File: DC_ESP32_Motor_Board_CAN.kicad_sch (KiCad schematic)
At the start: 44 parts, among them IC1 VNH7100BASTR, IC2 TJA1050T_CM, IC3 LSM6DS3TR-C, J1 SM04B-SRSS-TB, J2 SM04B-SRSS-TB, J3 XT30PB, J4 XT30PB, J5 SM04B-SRSS-TB, J6 SM04B-SRSS-TB, J7 XT30PB, J8 Conn_01x03_Pin, Q1 BSS138, Q2 BSS138, SW1 DSHP04TJGER, U1 MOUDLE-SEEEDUINO-XIAO-ESP32C3

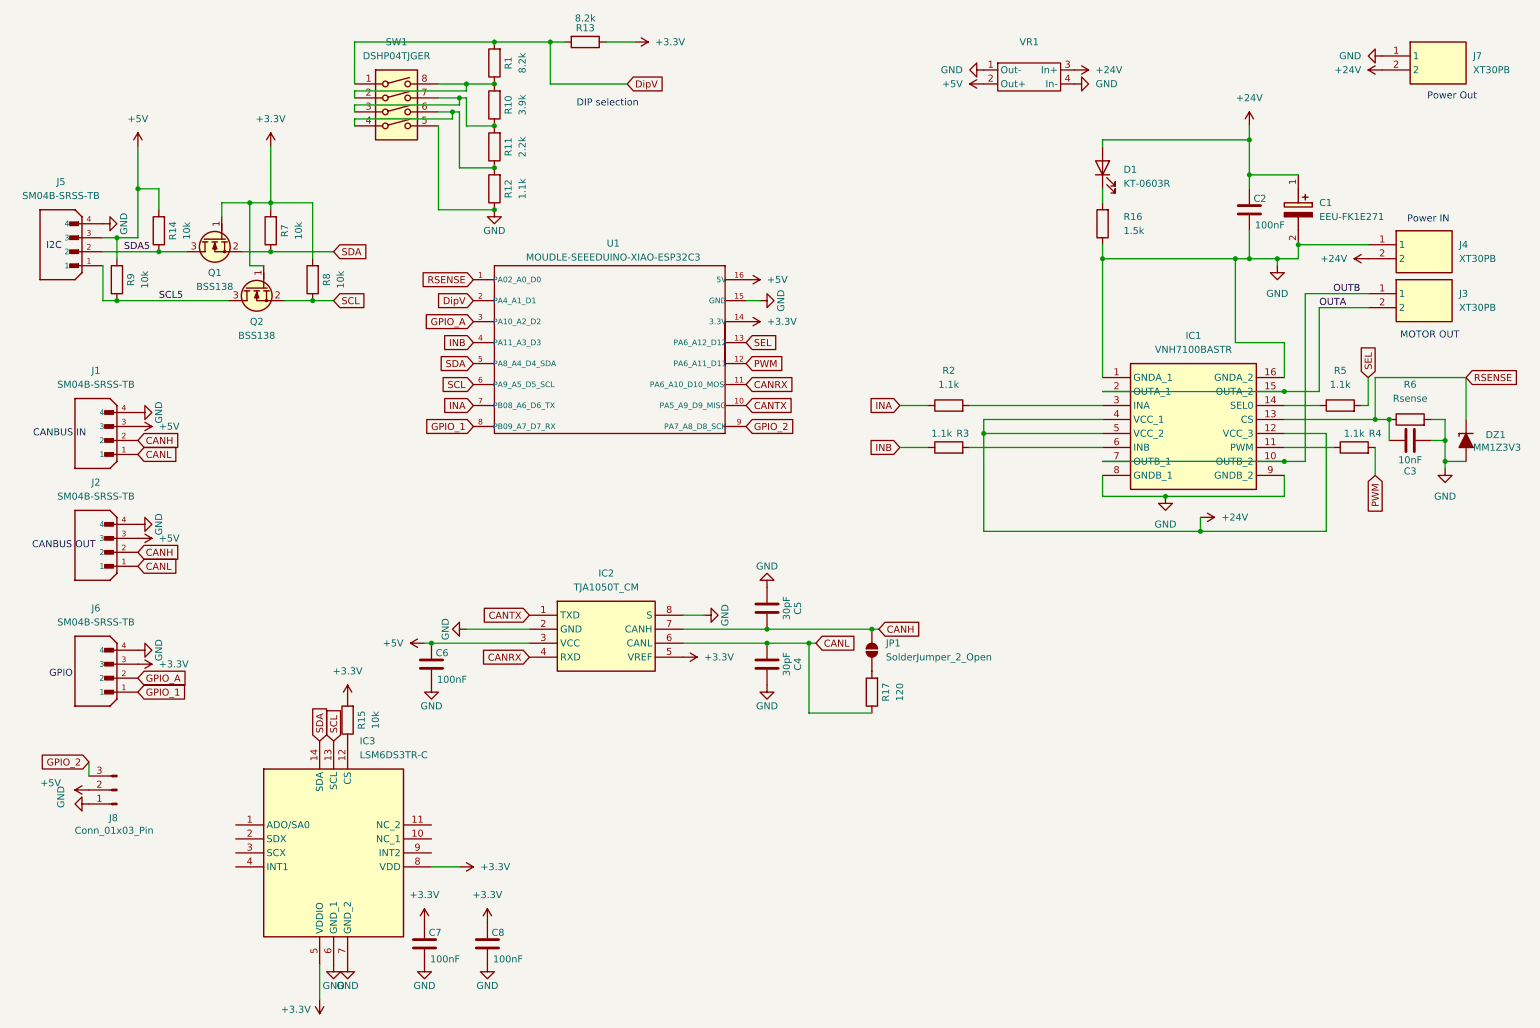
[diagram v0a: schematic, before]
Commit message: Updates for PCB
Bigger GPIO2
Added RGB LED
Updated xt30s
Updated xt30 size to fit inline connectors on PCB
Fixed jst sh connections
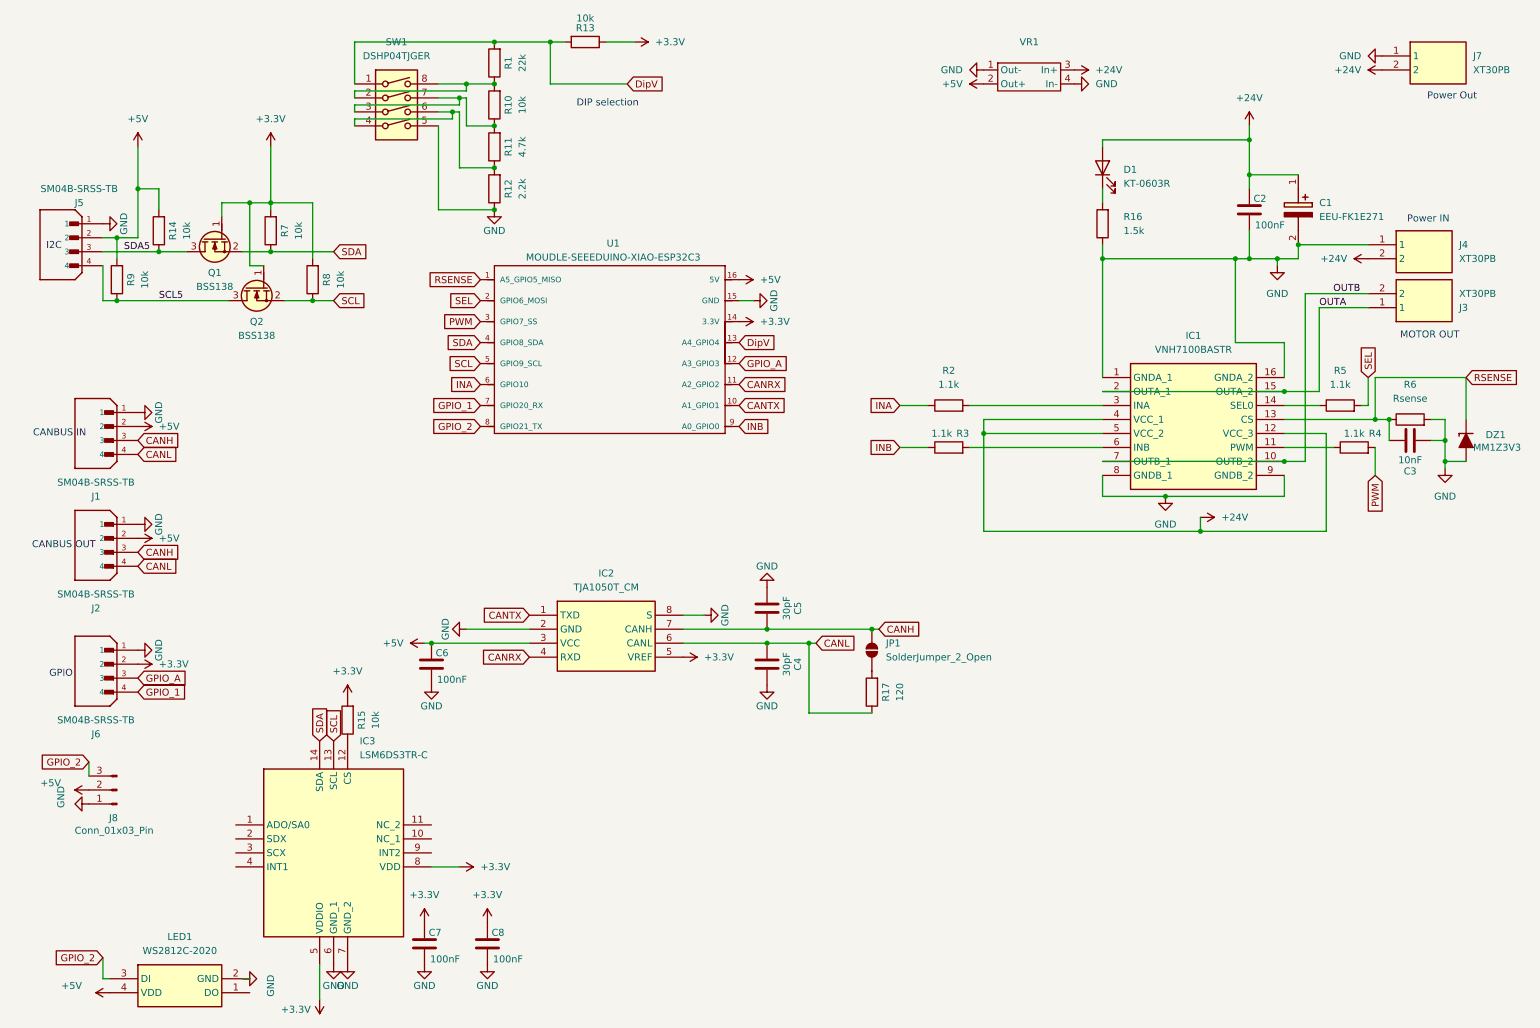
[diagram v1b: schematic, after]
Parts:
- added LED1: WS2812C-2020, WS2812C2020, symbol SamacSys_Parts:WS2812C-2020
- J3: footprint Library:Xt30 Horizontal -> JST_Sorted:Xt30 Female 90 1 mount removed
- J8: footprint Connector_PinHeader_1.00mm:PinHeader_1x03_P1.00mm_Vertical -> Connector_PinHeader_2.54mm:PinHeader_1x03_P2.54mm_Vertical
- R1: value 8.2k -> 22k
- R10: value 3.9k -> 10k
- R11: value 2.2k -> 4.7k
- R12: value 1.1k -> 2.2k
- R13: value 8.2k -> 10k
- U1: footprint Arduino:ESP32-C3 16 Pin Super Mini -> Arduino:MOUDLE14P-SMD-2.54-21X17.8MM; symbol SamacSys_Parts:MOUDLE-SEEEDUINO-XIAO-ESP32C3 -> SamacSys_Parts:ESP32_C3_Super_mini; now in the parts list
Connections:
- net +3.3V: now also J6.2; no longer J6.3
- net +5V: now also J1.2, J2.2, J5.2, LED1.4 (VDD); no longer J1.3, J2.3, J5.3
- net CANH: now also J1.3, J2.3; no longer J1.2, J2.2
- net CANL: now also J1.4, J2.4; no longer J1.1, J2.1
- net DipV: now also U1.13 (A4_GPIO4); no longer U1.2 (PA4_A1_D1)
- net GND: now also J1.1, J2.1, J5.1, J6.1, LED1.2 (GND); no longer J1.4, J2.4, J5.4, J6.4
- net GPIO_1: now also J6.4, U1.7 (GPIO20_RX); no longer J6.1, U1.8 (PB09_A7_D7_RX)
- net GPIO_2: now also U1.8 (GPIO21_TX), LED1.3 (DI); no longer U1.9 (PA7_A8_D8_SCK)
- net GPIO_A: now also J6.3, U1.12 (A3_GPIO3); no longer J6.2, U1.3 (PA10_A2_D2)
- net INA: now also U1.6 (GPIO10); no longer U1.7 (PB08_A6_D6_TX)
- net INB: now also U1.9 (A0_GPIO0); no longer U1.4 (PA11_A3_D3)
- net OUTA: now also J3.1; no longer J3.2
- net OUTB: now also J3.2; no longer J3.1
- net PWM: now also U1.3 (GPIO7_SS); no longer U1.12 (PA6_A11_D11)
- net SCL: now also U1.5 (GPIO9_SCL); no longer U1.6 (PA9_A5_D5_SCL)
- net SCL5: now also J5.4; no longer J5.1
- net SDA: now also U1.4 (GPIO8_SDA); no longer U1.5 (PA8_A4_D4_SDA)
- net SDA5: now also J5.3; no longer J5.2
- net SEL: now also U1.2 (GPIO6_MOSI); no longer U1.13 (PA6_A12_D12)
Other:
- moved on the sheet: J1, J2, J6

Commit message: Newest Update for Review
Updated do not place parts, and fixed last last few traces. Should be good for ordering
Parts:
- added D2: SS34, Diode_SMD:D_SOD-123, symbol Diode:1N5820
- added JP2: SolderJumper_2_Open, CutomParts:Jumper Connected 2 Pin Small, symbol Jumper:SolderJumper_2_Bridged
- J3: footprint JST_Sorted:Xt30 Female 90 1 mount removed -> JST_Sorted:xt30_90_Female
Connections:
- net +24V: now also D2.2 (A); no longer VR1.3 (In+)
- net at R16.2: now also JP2.1 (A); no longer D1.1 (K)
- new net: D1.1 (K), JP2.2 (B)
- new net: D2.1 (K), VR1.3 (In+)
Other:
- moved on the sheet: D1, R16
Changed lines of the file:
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@@
 	(wire
 		(pts
-			(xy 208.28 35.56) (xy 208.28 36.83)
+			(xy 214.63 39.37) (xy 226.06 35.56)
 		)
 		(stroke
@@
 	(wire
 		(pts
-			(xy 208.28 35.56) (xy 234.95 35.56)
+			(xy 208.28 22.86) (xy 203.2 22.86)
 		)
 		(stroke
@@
 	(wire
 		(pts
+			(xy 226.06 35.56) (xy 234.95 35.56)
+		)
+		(stroke
+			(width 0)
+			(type default)
+		)
+	)
+	(wire
+		(pts
 			(xy 66.04 191.77) (xy 66.04 185.42)
 		)
@@
 	(wire
 		(pts
-			(xy 72.39 26.67) (xy 92.71 26.67)
+			(xy 200.66 54.61) (xy 196.85 54.61)
 		)
 		(stroke
@@
 	(wire
 		(pts
-			(xy 267.97 86.36) (xy 270.51 86.36)
+			(xy 72.39 26.67) (xy 92.71 26.67)
 		)
 		(stroke
@@
 	(wire
 		(pts
-			(xy 87.63 25.4) (xy 92.71 25.4)
+			(xy 267.97 86.36) (xy 270.51 86.36)
 		)
 		(stroke
@@
 	(wire
 		(pts
-			(xy 208.28 78.74) (xy 208.28 57.15)
+			(xy 87.63 25.4) (xy 92.71 25.4)
 		)
 		(stroke
@@
 	(wire
 		(pts
-			(xy 208.28 100.33) (xy 219.71 100.33)
+			(xy 208.28 78.74) (xy 208.28 57.15)
 		)
 		(stroke
@@
 	(wire
 		(pts
-			(xy 184.15 91.44) (xy 208.28 91.44)
+			(xy 208.28 100.33) (xy 219.71 100.33)
 		)
 		(stroke
@@
 	(wire
 		(pts
-			(xy 208.28 44.45) (xy 208.28 46.99)
+			(xy 184.15 91.44) (xy 208.28 91.44)
 		)
 		(stroke
@@
 	(wire
 		(pts
+			(xy 196.85 54.61) (xy 196.85 50.8)
+		)
+		(stroke
+			(width 0)
+			(type default)
+		)
+	)
+	(wire
+		(pts
 			(xy 208.28 57.15) (xy 232.41 57.15)
 		)
@@
 	(wire
 		(pts
+			(xy 196.85 39.37) (xy 196.85 43.18)
+		)
+		(stroke
+			(width 0)
+			(type default)
+		)
+	)
+	(wire
+		(pts
 			(xy 240.03 57.15) (xy 240.03 58.42)
 		)
@@
 	(wire
 		(pts
+			(xy 219.71 22.86) (xy 215.9 22.86)
+		)
+		(stroke
+			(width 0)
+			(type default)
+		)
+	)
+	(wire
+		(pts
 			(xy 29.21 53.34) (xy 26.67 53.34)
 		)
@@
 	(wire
 		(pts
+			(xy 196.85 39.37) (xy 207.01 39.37)
+		)
+		(stroke
+			(width 0)
+			(type default)
+		)
+	)
+	(wire
+		(pts
 			(xy 64.77 57.15) (xy 64.77 46.99)
 		)
@@
 		)
 	)
+	(netclass_flag ""
+		(length 2.54)
+		(shape round)
+		(at 204.47 22.86 0)
+		(fields_autoplaced yes)
+		(effects
+			(font
+				(size 1.27 1.27)
+			)
+			(justify left bottom)
+		)
+		(property "Netclass" "Low Power"
+			(at 205.1685 20.32 0)
+			(effects
+				(font
+					(size 1.27 1.27)
+					(italic yes)
+				)
+				(justify left)
+			)
+		)
+	)
 	(symbol
 		(lib_id "Connector:Conn_01x03_Pin")
@@
 	(symbol
 		(lib_id "power:+24V")
-		(at 203.2 22.86 270)
+		(at 219.71 22.86 270)
 		(unit 1)
 		(exclude_from_sim no)
@@
 		(fields_autoplaced yes)
 		(property "Reference" "#PWR033"
-			(at 199.39 22.86 0)
+			(at 215.9 22.86 0)
 			(effects
 				(font
@@
 		)
 		(property "Value" "+24V"
-			(at 207.01 22.86 90)
+			(at 223.52 22.86 90)
 			(effects
 				(font
@@
 		)
 		(property "Footprint" ""
-			(at 203.2 22.86 0)
+			(at 219.71 22.86 0)
 			(effects
 				(font
@@
 		)
 		(property "Datasheet" ""
-			(at 203.2 22.86 0)
+			(at 219.71 22.86 0)
 			(effects
 				(font
@@
 		)
 		(property "Description" ""
-			(at 203.2 22.86 0)
+			(at 219.71 22.86 0)
 			(effects
 				(font
@@
 	)
 	(symbol
+		(lib_id "Jumper:SolderJumper_2_Bridged")
+		(at 196.85 46.99 90)
+		(unit 1)
+		(exclude_from_sim yes)
+		(in_bom no)
+		(on_board yes)
+		(dnp no)
+		(property "Reference" "JP2"
+			(at 191.516 46.99 90)
+			(effects
+				(font
+					(size 1.27 1.27)
+				)
+				(justify right)
+			)
+		)
+		(property "Value" "SolderJumper_2_Open"
+			(at 174.752 48.768 90)
+			(effects
+				(font
+					(size 1.27 1.27)
+				)
+				(justify right)
+			)
+		)
+		(property "Footprint" "CutomParts:Jumper Connected 2 Pin Small"
+			(at 196.85 46.99 0)
+			(effects
+				(font
+					(size 1.27 1.27)
+				)
+				(hide yes)
+			)
+		)
+		(property "Datasheet" "~"
+			(at 196.85 46.99 0)
+			(effects
+				(font
+					(size 1.27 1.27)
+				)
+				(hide yes)
+			)
+		)
+		(property "Description" "Solder Jumper, 2-pole, closed/bridged"
+			(at 196.85 46.99 0)
+			(effects
+				(font
+					(size 1.27 1.27)
+				)
+				(hide yes)
+			)
+		)
+		(pin "2"
+		)
+		(pin "1"
+		)
+		(instances
+			(project "DC_ESP32_Motor_Board_CAN"
+				(path "/7e6422eb-c3b1-4c4a-b69f-f4b10fde7fbc"
+					(reference "JP2")
+					(unit 1)
+				)
+			)
+		)
+	)
+	(symbol
 		(lib_id "Device:C")
 		(at 147.32 120.65 180)
@@
 	(symbol
 		(lib_id "Device:R")
-		(at 208.28 50.8 180)
+		(at 204.47 54.61 270)
 		(unit 1)
 		(exclude_from_sim no)
@@
 		(dnp no)
 		(property "Reference" "R16"
-			(at 212.09 49.53 0)
+			(at 206.502 52.324 90)
 			(effects
 				(font
@@
 		)
 		(property "Value" "1.5k"
-			(at 212.09 52.07 0)
+			(at 206.502 49.784 90)
 			(effects
 				(font
@@
 		)
 		(property "Footprint" "Resistor_SMD:R_0402_1005Metric"
-			(at 210.058 50.8 90)
+			(at 204.47 52.832 90)
 			(effects
 				(font
@@
 		)
 		(property "Datasheet" "~"
-			(at 208.28 50.8 0)
+			(at 204.47 54.61 0)
 			(effects
 				(font
@@
 		)
 		(property "Description" ""
-			(at 208.28 50.8 0)
+			(at 204.47 54.61 0)
 			(effects
 				(font
@@
 	(symbol
 		(lib_id "Device:LED")
-		(at 208.28 40.64 90)
+		(at 210.82 39.37 0)
 		(unit 1)
 		(exclude_from_sim no)
@@
 		(fields_autoplaced yes)
 		(property "Reference" "D1"
-			(at 212.09 40.9574 90)
+			(at 209.2325 33.02 0)
 			(effects
 				(font
 					(size 1.27 1.27)
 				)
-				(justify right)
 			)
 		)
 		(property "Value" "KT-0603R"
-			(at 212.09 43.4974 90)
+			(at 209.2325 35.56 0)
 			(effects
 				(font
 					(size 1.27 1.27)
 				)
-				(justify right)
 			)
 		)
 		(property "Footprint" "LED_SMD:LED_0603_1608Metric"
-			(at 208.28 40.64 0)
+			(at 210.82 39.37 0)
 			(effects
 				(font
@@
 		)
 		(property "Datasheet" "~"
-			(at 208.28 40.64 0)
+			(at 210.82 39.37 0)
 			(effects
 				(font
@@
 		)
 		(property "Description" "Light emitting diode"
-			(at 208.28 40.64 0)
+			(at 210.82 39.37 0)
 			(effects
 				(font
@@
 	)
 	(symbol
+		(lib_id "Diode:1N5820")
+		(at 212.09 22.86 0)
+		(unit 1)
+		(exclude_from_sim no)
+		(in_bom yes)
+		(on_board yes)
+		(dnp no)
+		(fields_autoplaced yes)
+		(property "Reference" "D2"
+			(at 211.7725 16.51 0)
+			(effects
+				(font
+					(size 1.27 1.27)
+				)
+			)
+		)
+		(property "Value" "SS34"
+			(at 211.7725 19.05 0)
+			(effects
+				(font
+					(size 1.27 1.27)
+				)
+			)
+		)
+		(property "Footprint" "Diode_SMD:D_SOD-123"
+			(at 212.09 27.305 0)
+			(effects
+				(font
+					(size 1.27 1.27)
+				)
+				(hide yes)
+			)
+		)
+		(property "Datasheet" "http://www.vishay.com/docs/88526/1n5820.pdf"
+			(at 212.09 22.86 0)
+			(effects
+				(font
+					(size 1.27 1.27)
+				)
+				(hide yes)
+			)
+		)
+		(property "Description" "20V 3A Schottky Barrier Rectifier Diode, DO-201AD"
+			(at 212.09 22.86 0)
+			(effects
+				(font
+					(size 1.27 1.27)
+				)
+				(hide yes)
+			)
+		)
+		(pin "1"
+		)
+		(pin "2"
+		)
+		(instances
+			(project "DC_ESP32_Motor_Board_CAN"
+				(path "/7e6422eb-c3b1-4c4a-b69f-f4b10fde7fbc"
+					(reference "D2")
+					(unit 1)
+				)
+			)
+		)
+	)
+	(symbol
 		(lib_id "Jumper:SolderJumper_2_Open")
 		(at 166.37 128.27 90)
@@
 			)
 		)
-		(property "Footprint" "JST_Sorted:Xt30 Female 90 1 mount removed"
+		(property "Footprint" "JST_Sorted:xt30_90_Female"
 			(at 273.05 -28.88 0)
 			(effects
